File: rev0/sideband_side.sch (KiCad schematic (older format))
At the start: 22 parts, among them IC1 ECP5-BGA256, U8 USB3343

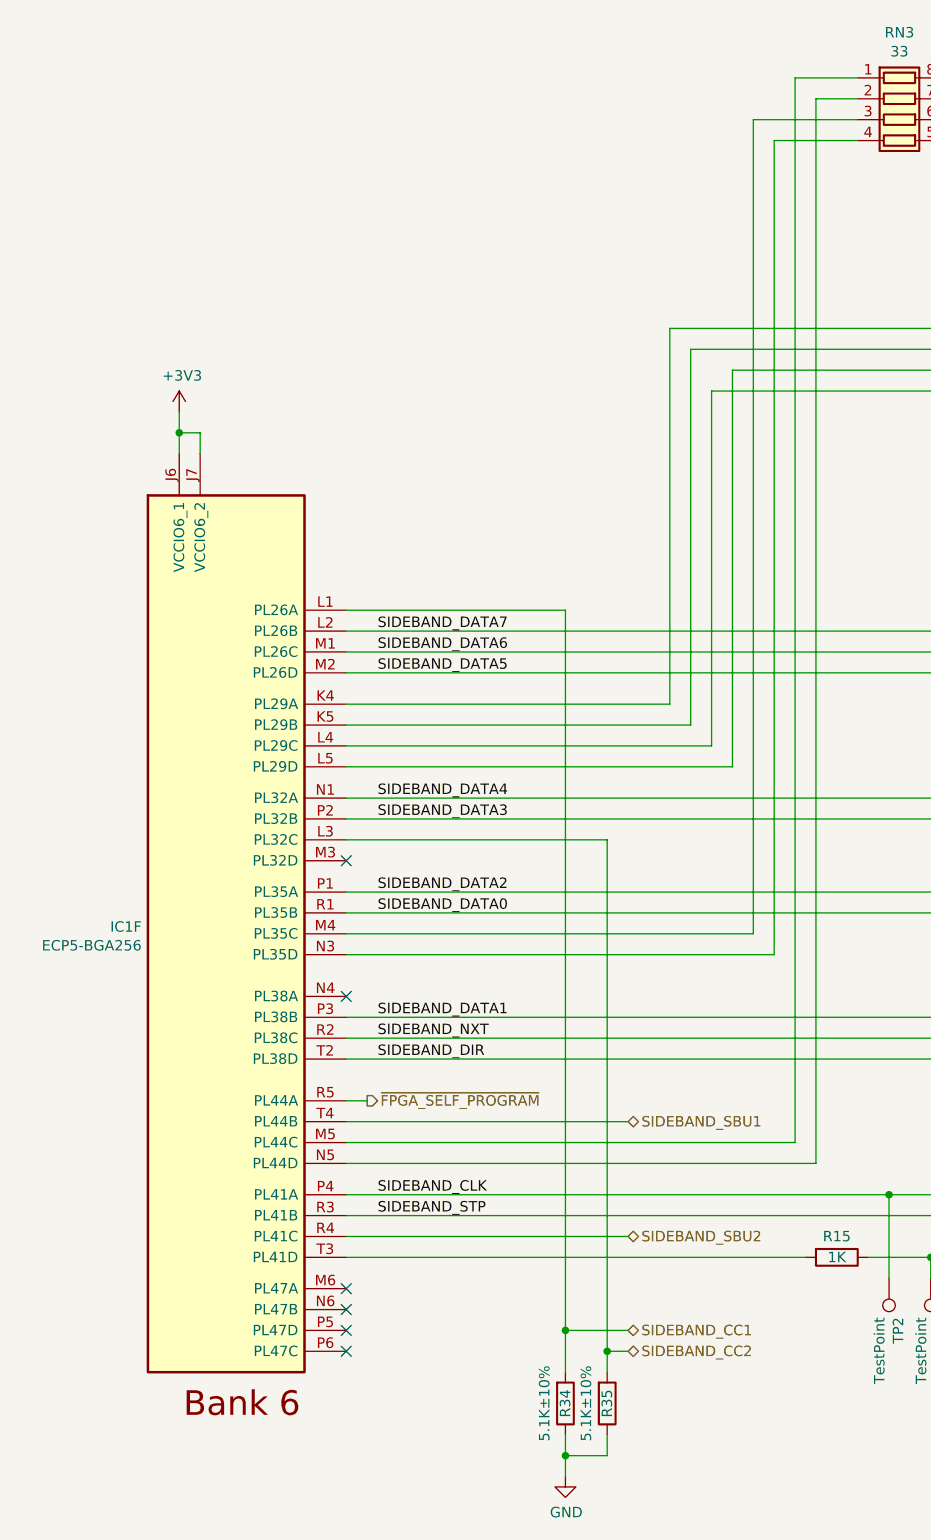
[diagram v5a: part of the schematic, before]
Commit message: hardware: update host/sideband CC signals
- add CC series resistors for reliable detection as sink when unpowered
- add PD capacitors
- update silkscreen to r0.3+
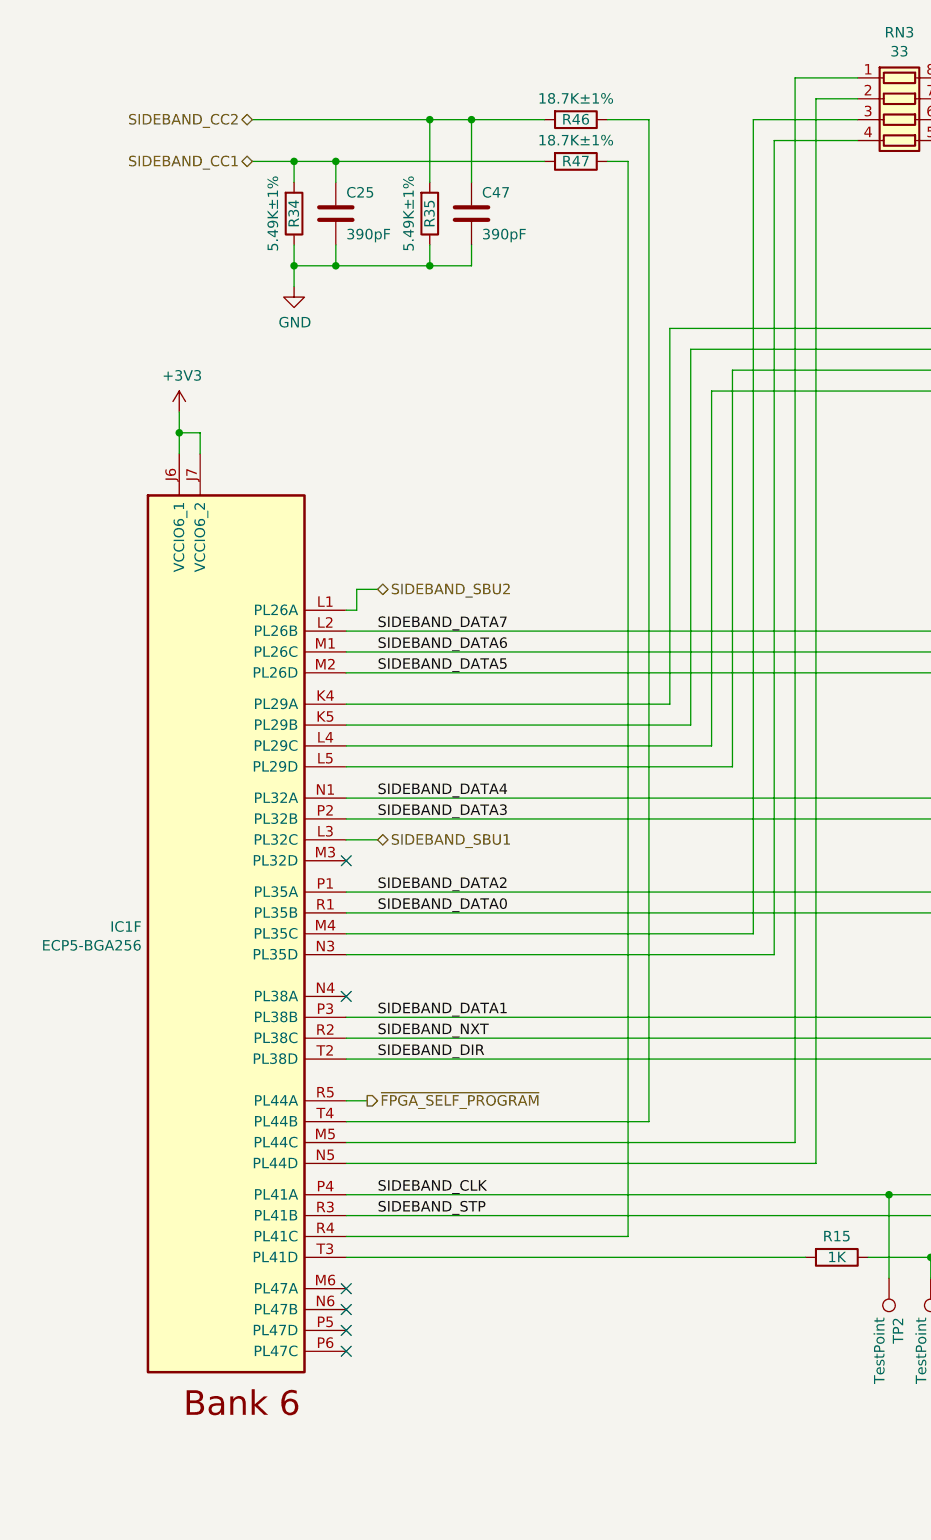
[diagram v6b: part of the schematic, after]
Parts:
- added C25, C47: 390pF, Capacitor_SMD:C_0402_1005Metric, symbol Device:C
- added R46, R47: 18.7K±1%, Resistor_SMD:R_0402_1005Metric, symbol Device:R
- R34, R35: value 5.1K±10% -> 5.49K±1%; Description (none) -> RES SMD 5.49K OHM 1% 1/10W 0402; Manufacturer (none) -> Panasonic; Part Number GENERIC-RES-0402-5.1K -> ERJ-2RKF5491X
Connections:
- net GND: now also C25.2, C47.2
- net SIDEBAND_CC1: now also C25.1, R47.2; no longer IC1.L1 (PL26A)
- net SIDEBAND_CC2: now also C47.1, R46.2; no longer IC1.L3 (PL32C)
- net SIDEBAND_SBU1: now also IC1.L3 (PL32C); no longer IC1.T4 (PL44B)
- net SIDEBAND_SBU2: now also IC1.L1 (PL26A); no longer IC1.R4 (PL41C)
- new net: IC1.R4 (PL41C), R47.1
- new net: IC1.T4 (PL44B), R46.1
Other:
- moved on the sheet: R34, R35
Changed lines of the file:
@@
 Sheet 2 9
 Title "LUNA: Sideband USB PHY"
-Date "2021-01-12"
+Date "2021-03-09"
 Rev "r0"
 Comp "Copyright 2019-2021 Great Scott Gadgets"
@@
 Wire Wire Line
 	2200 5750 2100 5750
-$Comp
-L Device:R R?
-U 1 1 60996F81
-P 3150 7200
-AR Path="/60996F81" Ref="R?"  Part="1"
-AR Path="/5DD754D4/60996F81" Ref="R?"  Part="1"
-AR Path="/5DCD9772/60996F81" Ref="R34"  Part="1"
-F 0 "R34" V 3150 7200 50  0000 C CNN
-F 1 "5.1K±10%" V 3050 7200 50  0000 C CNN
-F 2 "Resistor_SMD:R_0402_1005Metric" V 3080 7200 50  0001 C CNN
-F 3 "~" H 3150 7200 50  0001 C CNN
-F 4 "GENERIC-RES-0402-5.1K" H 3150 7200 50  0001 C CNN "Part Number"
-F 5 "any equivalent" H 3150 7200 50  0001 C CNN "Substitution"
-	1    3150 7200
-	1    0    0    1
-$EndComp
-$Comp
-L power:GND #PWR?
-U 1 1 60996F87
-P 3150 7550
-AR Path="/60996F87" Ref="#PWR?"  Part="1"
-AR Path="/5DD754D4/60996F87" Ref="#PWR?"  Part="1"
-AR Path="/5DCD9772/60996F87" Ref="#PWR010"  Part="1"
-F 0 "#PWR010" H 3150 7300 50  0001 C CNN
-F 1 "GND" H 3154 7378 50  0000 C CNN
-F 2 "" H 3150 7550 50  0001 C CNN
-F 3 "" H 3150 7550 50  0001 C CNN
-	1    3150 7550
-	1    0    0    -1
-$EndComp
-$Comp
-L Device:R R?
-U 1 1 60996F8E
-P 3350 7200
-AR Path="/60996F8E" Ref="R?"  Part="1"
-AR Path="/5DD754D4/60996F8E" Ref="R?"  Part="1"
-AR Path="/5DCD9772/60996F8E" Ref="R35"  Part="1"
-F 0 "R35" V 3350 7200 50  0000 C CNN
-F 1 "5.1K±10%" V 3250 7200 50  0000 C CNN
-F 2 "Resistor_SMD:R_0402_1005Metric" V 3280 7200 50  0001 C CNN
-F 3 "~" H 3350 7200 50  0001 C CNN
-F 4 "GENERIC-RES-0402-5.1K" H 3350 7200 50  0001 C CNN "Part Number"
-F 5 "any equivalent" H 3350 7200 50  0001 C CNN "Substitution"
-	1    3350 7200
-	1    0    0    1
-$EndComp
-Wire Wire Line
-	3150 7350 3150 7450
-Wire Wire Line
-	3150 7450 3350 7450
-Wire Wire Line
-	3350 7450 3350 7350
-Connection ~ 3150 7450
-Wire Wire Line
-	3150 7450 3150 7550
-Text HLabel 3450 6950 2    50   BiDi ~ 0
+Text HLabel 1650 1050 0    50   BiDi ~ 0
 SIDEBAND_CC2
 Text Label 2250 4400 0    50   ~ 0
@@
 Wire Wire Line
 	4300 6500 2100 6500
-Text HLabel 3450 6400 2    50   BiDi ~ 0
+Text HLabel 2250 3300 2    50   BiDi ~ 0
 SIDEBAND_SBU2
-Text HLabel 3450 5850 2    50   BiDi ~ 0
+Text HLabel 2250 4500 2    50   BiDi ~ 0
 SIDEBAND_SBU1
-Wire Wire Line
-	3450 5850 2100 5850
-Wire Wire Line
-	3450 6400 2100 6400
-Wire Wire Line
-	2100 4500 3350 4500
-Text HLabel 3450 6850 2    50   BiDi ~ 0
+Text HLabel 1650 1250 0    50   BiDi ~ 0
 SIDEBAND_CC1
-Wire Wire Line
-	2100 3400 3150 3400
-Wire Wire Line
-	3150 7050 3150 6850
-Wire Wire Line
-	3350 7050 3350 6950
 Text Label 7000 850  0    50   ~ 0
 PMOD_B0
@@
 Text Label 7700 650  0    50   ~ 0
 PMOD_B[0..7]
-Wire Wire Line
-	3350 6950 3450 6950
-Connection ~ 3350 6950
-Wire Wire Line
-	3350 6950 3350 4500
-Wire Wire Line
-	3450 6850 3150 6850
-Connection ~ 3150 6850
-Wire Wire Line
-	3150 6850 3150 3400
 Text Label 7000 1050 0    50   ~ 0
 PMOD_B2
@@
 	0    -1   -1   0
 $EndComp
+$Comp
+L Device:R R?
+U 1 1 60506CAE
+P 3200 1050
+AR Path="/60506CAE" Ref="R?"  Part="1"
+AR Path="/5DD754D4/60506CAE" Ref="R?"  Part="1"
+AR Path="/5DCD9772/60506CAE" Ref="R46"  Part="1"
+F 0 "R46" V 3200 1050 50  0000 C CNN
+F 1 "18.7K±1%" V 3100 1050 50  0000 C CNN
+F 2 "Resistor_SMD:R_0402_1005Metric" V 3130 1050 50  0001 C CNN
+F 3 "~" H 3200 1050 50  0001 C CNN
+F 4 "ERJ-2RKF1872X" H 3200 1050 50  0001 C CNN "Part Number"
+F 5 "any equivalent" H 3200 1050 50  0001 C CNN "Substitution"
+F 6 "RES SMD 18.7K OHM 1% 1/10W 0402" H 3200 1050 50  0001 C CNN "Description"
+F 7 "Panasonic" H 3200 1050 50  0001 C CNN "Manufacturer"
+	1    3200 1050
+	0    1    1    0
+$EndComp
+$Comp
+L Device:R R?
+U 1 1 60506CB6
+P 3200 1250
+AR Path="/60506CB6" Ref="R?"  Part="1"
+AR Path="/5DD754D4/60506CB6" Ref="R?"  Part="1"
+AR Path="/5DCD9772/60506CB6" Ref="R47"  Part="1"
+F 0 "R47" V 3200 1250 50  0000 C CNN
+F 1 "18.7K±1%" V 3100 1250 50  0000 C CNN
+F 2 "Resistor_SMD:R_0402_1005Metric" V 3130 1250 50  0001 C CNN
+F 3 "~" H 3200 1250 50  0001 C CNN
+F 4 "ERJ-2RKF1872X" H 3200 1250 50  0001 C CNN "Part Number"
+F 5 "any equivalent" H 3200 1250 50  0001 C CNN "Substitution"
+F 6 "RES SMD 18.7K OHM 1% 1/10W 0402" H 3200 1250 50  0001 C CNN "Description"
+F 7 "Panasonic" H 3200 1250 50  0001 C CNN "Manufacturer"
+	1    3200 1250
+	0    1    1    0
+$EndComp
+$Comp
+L Device:C C47
+U 1 1 6056F7FB
+P 2700 1500
+F 0 "C47" H 2750 1600 50  0000 L CNN
+F 1 "390pF" H 2750 1400 50  0000 L CNN
+F 2 "Capacitor_SMD:C_0402_1005Metric" H 2738 1350 50  0001 C CNN
+F 3 "~" H 2700 1500 50  0001 C CNN
+F 4 "GENERIC-CAP-0402-390pF" H 2700 1500 50  0001 C CNN "Part Number"
+F 5 "any equivalent" H 2700 1500 50  0001 C CNN "Substitution"
+	1    2700 1500
+	1    0    0    -1
+$EndComp
+Wire Wire Line
+	1850 1350 1850 1250
+Wire Wire Line
+	2500 1350 2500 1050
+Wire Wire Line
+	1850 1750 1850 1850
+Connection ~ 1850 1750
+Wire Wire Line
+	2500 1750 2500 1650
+Wire Wire Line
+	1850 1750 2050 1750
+Wire Wire Line
+	1850 1650 1850 1750
+$Comp
+L power:GND #PWR?
+U 1 1 60506C97
+P 1850 1850
+AR Path="/60506C97" Ref="#PWR?"  Part="1"
+AR Path="/5DD754D4/60506C97" Ref="#PWR?"  Part="1"
+AR Path="/5DCD9772/60506C97" Ref="#PWR010"  Part="1"
+F 0 "#PWR010" H 1850 1600 50  0001 C CNN
+F 1 "GND" H 1854 1678 50  0000 C CNN
+F 2 "" H 1850 1850 50  0001 C CNN
+F 3 "" H 1850 1850 50  0001 C CNN
+	1    1850 1850
+	1    0    0    -1
+$EndComp
+$Comp
+L Device:R R?
+U 1 1 60996F8E
+P 2500 1500
+AR Path="/60996F8E" Ref="R?"  Part="1"
+AR Path="/5DD754D4/60996F8E" Ref="R?"  Part="1"
+AR Path="/5DCD9772/60996F8E" Ref="R35"  Part="1"
+F 0 "R35" V 2500 1500 50  0000 C CNN
+F 1 "5.49K±1%" V 2400 1500 50  0000 C CNN
+F 2 "Resistor_SMD:R_0402_1005Metric" V 2430 1500 50  0001 C CNN
+F 3 "~" H 2500 1500 50  0001 C CNN
+F 4 "ERJ-2RKF5491X" H 2500 1500 50  0001 C CNN "Part Number"
+F 5 "any equivalent" H 2500 1500 50  0001 C CNN "Substitution"
+F 6 "RES SMD 5.49K OHM 1% 1/10W 0402" H 2500 1500 50  0001 C CNN "Description"
+F 7 "Panasonic" H 2500 1500 50  0001 C CNN "Manufacturer"
+	1    2500 1500
+	1    0    0    1
+$EndComp
+$Comp
+L Device:R R?
+U 1 1 60996F81
+P 1850 1500
+AR Path="/60996F81" Ref="R?"  Part="1"
+AR Path="/5DD754D4/60996F81" Ref="R?"  Part="1"
+AR Path="/5DCD9772/60996F81" Ref="R34"  Part="1"
+F 0 "R34" V 1850 1500 50  0000 C CNN
+F 1 "5.49K±1%" V 1750 1500 50  0000 C CNN
+F 2 "Resistor_SMD:R_0402_1005Metric" V 1780 1500 50  0001 C CNN
+F 3 "~" H 1850 1500 50  0001 C CNN
+F 4 "ERJ-2RKF5491X" H 1850 1500 50  0001 C CNN "Part Number"
+F 5 "any equivalent" H 1850 1500 50  0001 C CNN "Substitution"
+F 6 "RES SMD 5.49K OHM 1% 1/10W 0402" H 1850 1500 50  0001 C CNN "Description"
+F 7 "Panasonic" H 1850 1500 50  0001 C CNN "Manufacturer"
+	1    1850 1500
+	1    0    0    1
+$EndComp
+$Comp
+L Device:C C25
+U 1 1 605E8DFE
+P 2050 1500
+F 0 "C25" H 2100 1600 50  0000 L CNN
+F 1 "390pF" H 2100 1400 50  0000 L CNN
+F 2 "Capacitor_SMD:C_0402_1005Metric" H 2088 1350 50  0001 C CNN
+F 3 "~" H 2050 1500 50  0001 C CNN
+F 4 "GENERIC-CAP-0402-390pF" H 2050 1500 50  0001 C CNN "Part Number"
+F 5 "any equivalent" H 2050 1500 50  0001 C CNN "Substitution"
+	1    2050 1500
+	1    0    0    -1
+$EndComp
+Wire Wire Line
+	2700 1650 2700 1750
+Wire Wire Line
+	2700 1750 2500 1750
+Connection ~ 2500 1750
+Wire Wire Line
+	2050 1650 2050 1750
+Connection ~ 2050 1750
+Wire Wire Line
+	2050 1750 2500 1750
+Wire Wire Line
+	2700 1350 2700 1050
+Wire Wire Line
+	2700 1050 2500 1050
+Wire Wire Line
+	1850 1250 2050 1250
+Wire Wire Line
+	2050 1350 2050 1250
+Wire Wire Line
+	1850 1250 1650 1250
+Connection ~ 1850 1250
+Wire Wire Line
+	1650 1050 2500 1050
+Connection ~ 2500 1050
+Wire Wire Line
+	3450 6400 3450 1250
+Wire Wire Line
+	3050 1250 2050 1250
+Connection ~ 2050 1250
+Wire Wire Line
+	2700 1050 3050 1050
+Connection ~ 2700 1050
+Wire Wire Line
+	3350 1050 3550 1050
+Wire Wire Line
+	3450 1250 3350 1250
+Wire Wire Line
+	2100 3400 2150 3400
+Wire Wire Line
+	2150 3400 2150 3300
+Wire Wire Line
+	2150 3300 2250 3300
+Wire Wire Line
+	2100 4500 2250 4500
+Wire Wire Line
+	3450 6400 2100 6400
+Wire Wire Line
+	2100 5850 3550 5850
 Wire Bus Line
 	7550 650  7550 2450
 Wire Bus Line
 	6050 3300 6050 6600
+Wire Wire Line
+	3550 5850 3550 1050
 $EndSCHEMATC

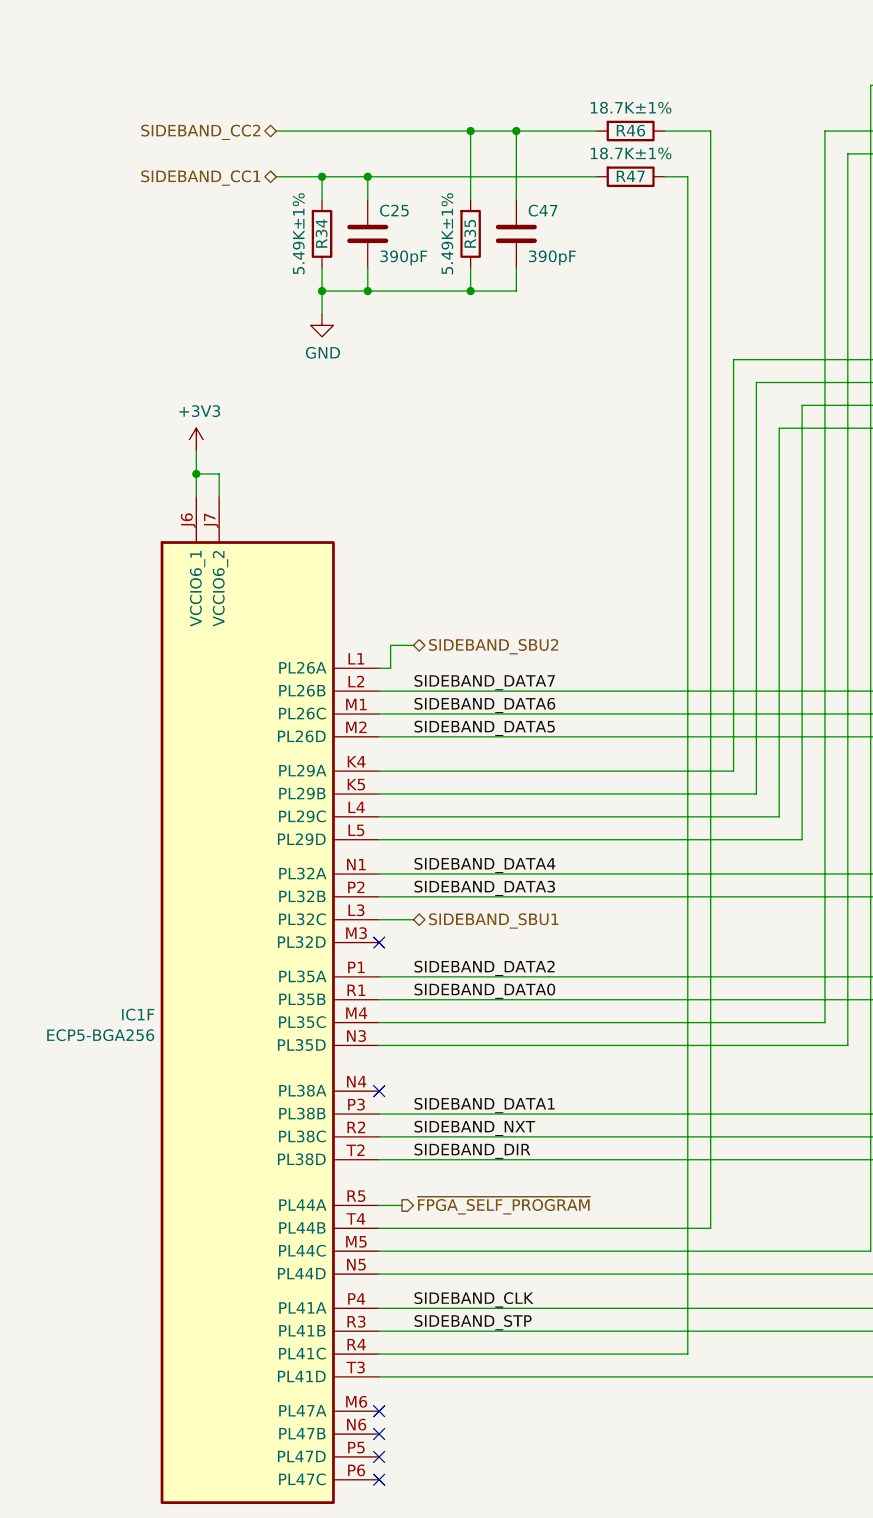
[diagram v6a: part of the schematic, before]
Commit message: hardware: update target CC signals
- add CC series resistors for reliable detection as sink when unpowered
- add PD capacitors
- add PD output driver
- add Rp (source mode) switch
- add CC test points for all Type-C ports
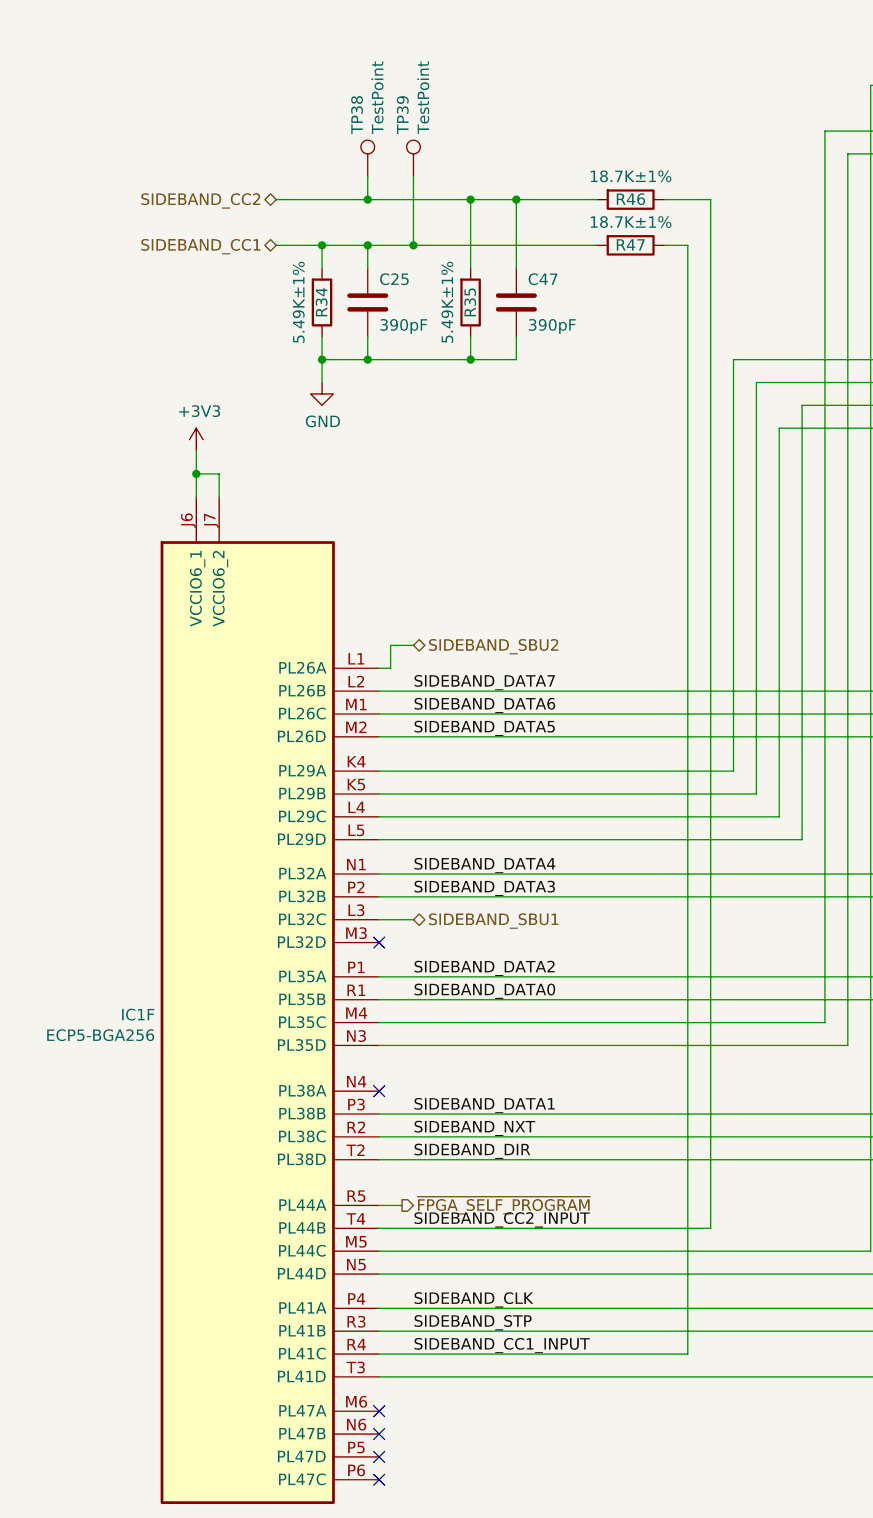
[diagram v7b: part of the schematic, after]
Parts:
- added TP38, TP39: TestPoint, TestPoint:TestPoint_Pad_D1.0mm, symbol Connector:TestPoint
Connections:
- net SIDEBAND_CC1: now also TP39.1
- net SIDEBAND_CC2: now also TP38.1
- net SIDEBAND_CC1_INPUT: now reaches IC1.R4 (PL41C), R47.1
- net SIDEBAND_CC2_INPUT: now reaches IC1.T4 (PL44B), R46.1
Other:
- moved on the sheet: C25, C47, R34, R35, R46, R47
